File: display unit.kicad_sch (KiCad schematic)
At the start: 1 part

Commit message: disp changes
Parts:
- added D? (x56): LED, symbol Device:LED
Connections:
- new net: D?.1 (K), D?.2 (A) (x16)
- new net: D?.1 (K), D?.2 (A), D?.2 (A) (x8)
- new net: D?.1 (K), D?.1 (K) (x8)
- new net: D?.2 (A), D?.2 (A) (x8)
- new net: D?.1 (K), D?.1 (K), D?.2 (A) (x8)
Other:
- moved on the sheet: U?

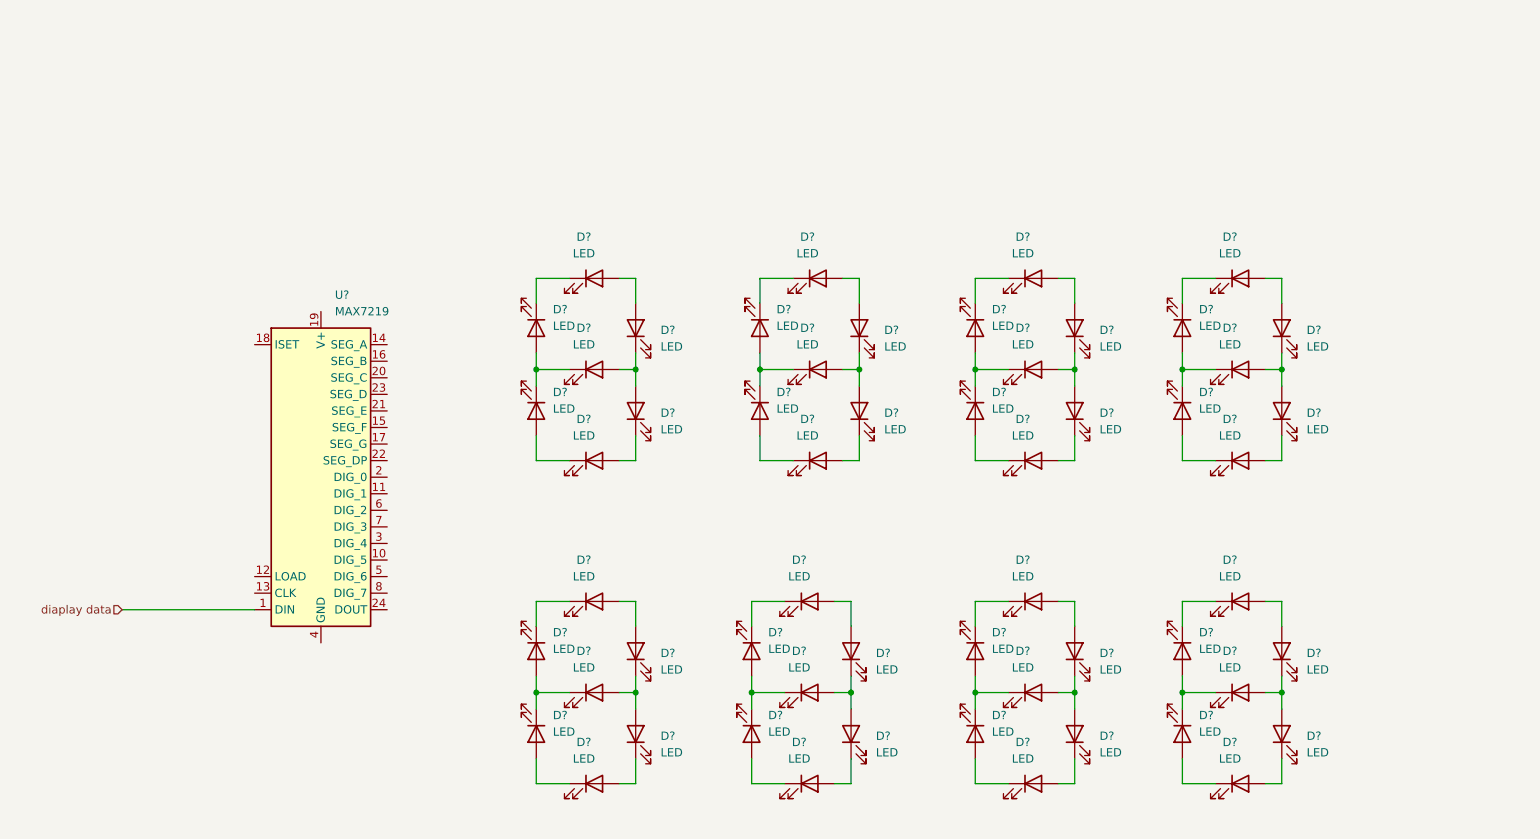
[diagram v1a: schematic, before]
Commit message: added display
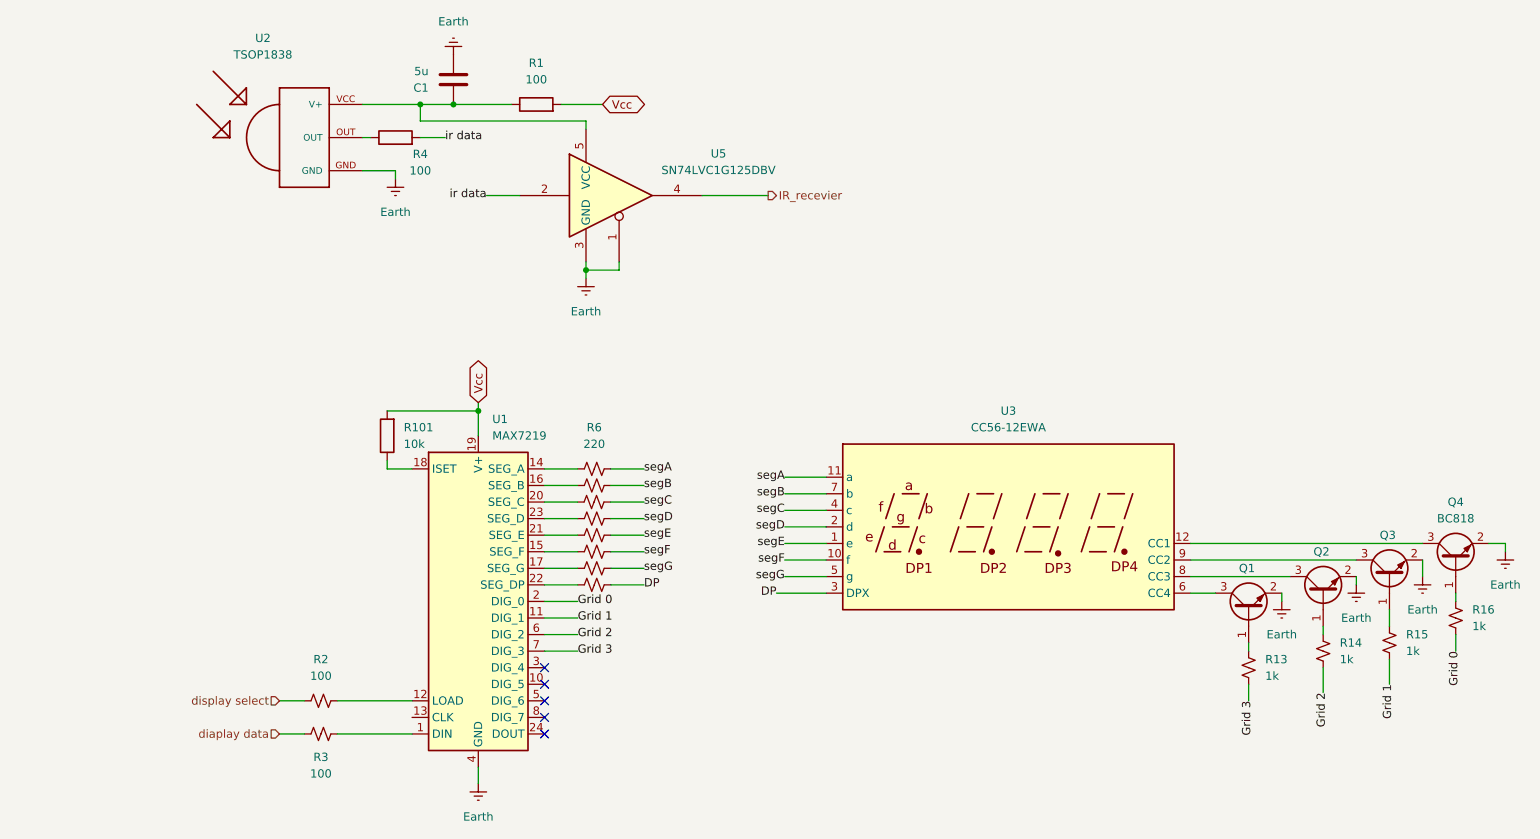
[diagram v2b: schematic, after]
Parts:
- removed D? (x56): LED, symbol Device:LED
- added C1: 5u, symbol Device:C
- added Q1, Q2, Q3, Q4: BC818, Package_TO_SOT_SMD:SOT-23, symbol Transistor_BJT:BC818
- added R1, R4: 100, symbol Device:R
- added R10, R11, R12, R5, R6, R7, R8, R9: 220, symbol Device:R_Small_US
- added R101: 10k, symbol Device:R
- added R13, R14, R15, R16: 1k, symbol Device:R_Small_US
- added R2, R3: 100, symbol Device:R_Small_US
- added U2: TSOP1838, TSOP18xx:TSOP18XX, symbol TSOP1838:TSOP1838
- added U3: CC56-12EWA, Display_7Segment:CA56-12EWA, symbol Display_Character:CC56-12EWA
- added U5: SN74LVC1G125DBV, Package_TO_SOT_SMD:SOT-23-5, symbol 74xGxx:SN74LVC1G125DBV
- gave numbers to parts that had none: 1
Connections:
- net diaplay data: now also R3.1; no longer U1.1 (DIN)
- net Grid 1: now reaches U1.11 (DIG_1)
- net Grid 1: now also R15.2
- net at U1.12 (LOAD): now also R2.2
- net at U1.14 (SEG_A): now also R6.1
- net at U1.15 (SEG_F): now also R10.1
- net at U1.16 (SEG_B): now also R7.1
- net at U1.17 (SEG_G): now also R11.1
- net at U1.18 (ISET): now also R101.1
- net Vcc: now reaches U1.19 (V+)
- net Vcc: now also R1.2, R101.2
- net Grid 0: now reaches U1.2 (DIG_0)
- net Grid 0: now also R16.2
- net at U1.20 (SEG_C): now also R5.1
- net at U1.21 (SEG_E): now also R9.1
- net at U1.22 (SEG_DP): now also R12.1
- net at U1.23 (SEG_D): now also R8.1
- net Earth: now reaches U1.4 (GND), U1.9 (GND)
- net Earth: now also C1.2, Q1.2 (E), Q2.2 (E), Q3.2 (E), Q4.2 (E), U2.GND, U5.1, U5.3 (GND)
- net Grid 2: now reaches U1.6 (DIG_2)
- net Grid 2: now also R14.2
- net Grid 3: now reaches U1.7 (DIG_3)
- net Grid 3: now also R13.2
- new net: Q1.1 (B), R13.1
- new net: R4.1, U2.OUT
- new net: C1.1, R1.1, U2.VCC (V+), U5.5 (VCC)
- new net: Q1.3 (C), U3.6 (CC4)
- new net: Q4.3 (C), U3.12 (CC1)
- new net: Q2.3 (C), U3.8 (CC3)
- new net: Q3.3 (C), U3.9 (CC2)
- new net: Q2.1 (B), R14.1
- new net: R3.2, U1.1 (DIN)
- new net: Q4.1 (B), R16.1
- new net: Q3.1 (B), R15.1
- new net DP: R12.2, U3.3 (DPX)
- new net IR_recevier: U5.4
- new net display select: R2.1
- new net ir data: R4.2, U5.2
- new net segA: R6.2, U3.11 (a)
- new net segB: R7.2, U3.7 (b)
- new net segC: R5.2, U3.4 (c)
- new net segD: R8.2, U3.2 (d)
- new net segE: R9.2, U3.1 (e)
- new net segF: R10.2, U3.10 (f)
- new net segG: R11.2, U3.5 (g)
- no-connect marks 0 -> 5
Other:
- moved on the sheet: U1
